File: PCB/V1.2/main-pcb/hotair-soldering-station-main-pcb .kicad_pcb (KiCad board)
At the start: 2 copper layers, 100 x 70 mm, 146 parts, among them J1 230VAC_IN, J10 T12_power (NS-25 r2,54), J11 LCD_CON2 (JST r.2.0), J12 LCD_CON1 (JST r.2.0), J13 ICP (goldpin r2,54), J14 Unused_GPIO, J2 FRONT_PANEL (IDC r. 2,54), J3 EARTH_GND, J4 24V_IN (NS-25 r2,54), J5 PSUPPLY (PWZ-02S r.3,96), J6 HOTAIR_FAN (JST r,2,54), J7 HOTAIR_MEAS (JST r.2,5), J8 HOTAIR_HEATER (PWZ-02S r.3,96), J9 WEP (r.2,54), Q1 BC817, Q10 RFP15P05, Q11 BC817, Q12 BC817, Q13 BC817, Q14 BC807, Q15 RFP15P05, Q2 BC807, Q3 BC817, Q4 RFP15P05, Q5 BC817, Q6 BT139-600, Q7 BC817, Q8 BC807, Q9 BC817, U1 MOC3041M, U2 MAX31855KASA, U3 MP1584-Step-Down, U4 AP1117-ADJ, U5 LM741, U6 AD8606, U8 STM32F103C6Tx

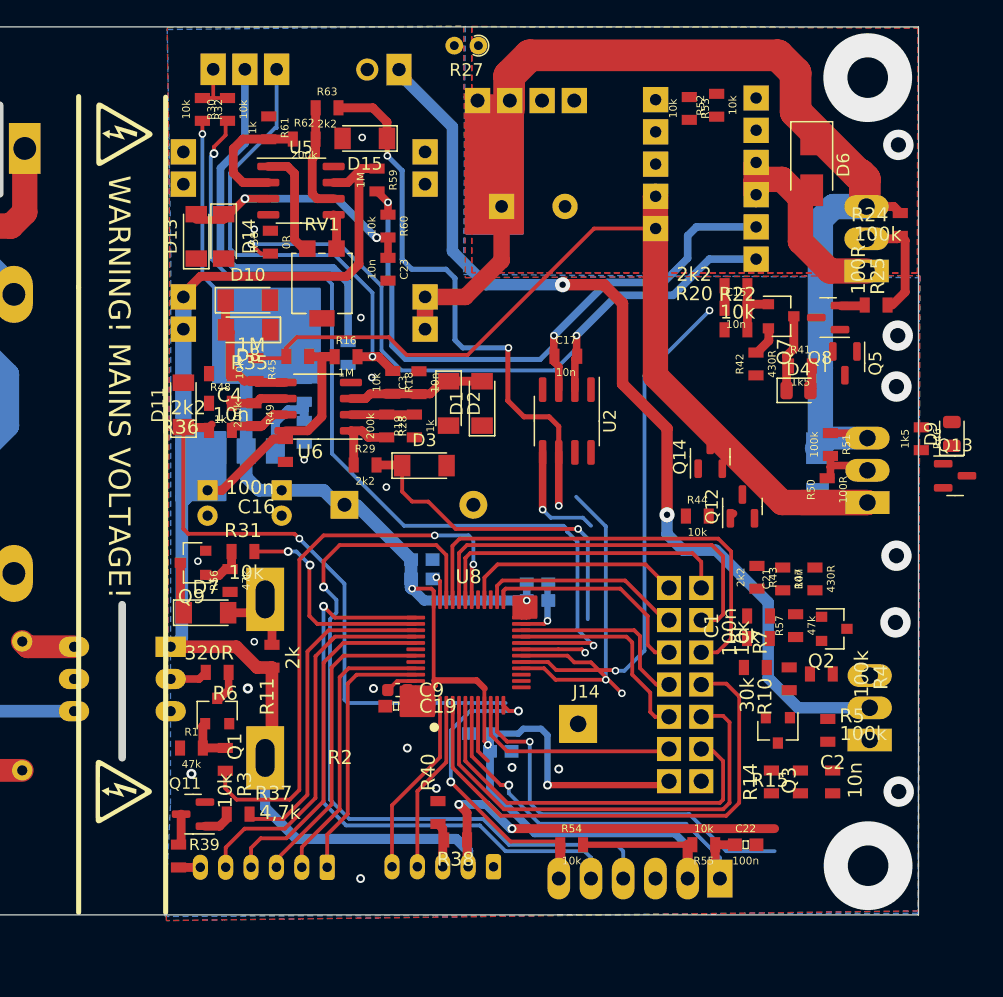
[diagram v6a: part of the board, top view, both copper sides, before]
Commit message: Routing PCB done, resolving DRC violations
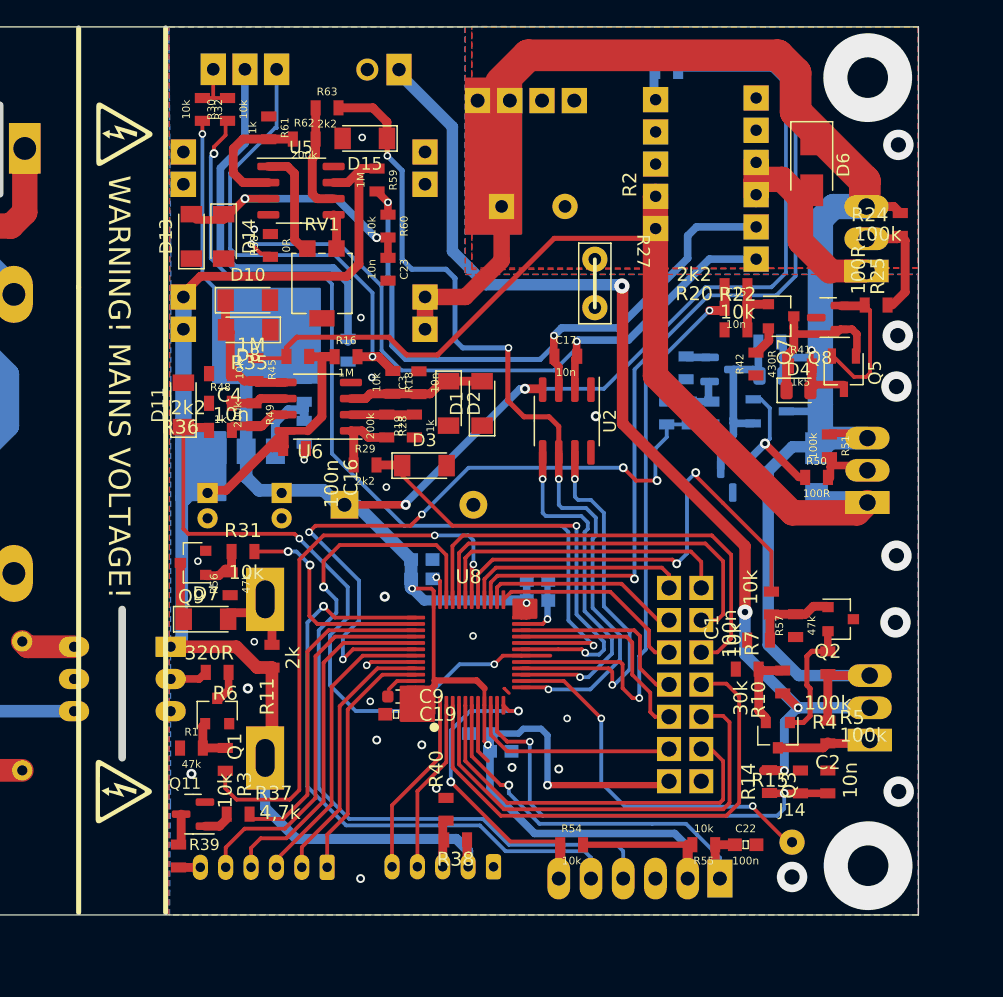
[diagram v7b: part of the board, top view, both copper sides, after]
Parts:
- C21, D9, Q12, Q14, R43, R44, R46, R47, R52, R53: moved to B.Cu
- J14: footprint My-Footprints:WIRE_PAD_1,3mm -> Wire_Pads:SolderWirePad_single_0-8mmDrill
- Q13: footprint Package_TO_SOT_SMD:SOT-23 -> Package_TO_SOT_SMD:TSOT-23; moved to B.Cu
- Q5: footprint Package_TO_SOT_SMD:SOT-23 -> Package_TO_SOT_SMD:TSOT-23
- R27: footprint Resistor_THT:R_Axial_DIN0204_L3.6mm_D1.6mm_P1.90mm_Vertical -> My-Footprints:ShortWire
- moved G*** 43.5 mm to (88.8, 46.6)
- moved G*** 26.4 mm to (76.3, 45.0)
- moved R47 19.5 mm to (98.7, 39.9)
- moved J14 19.3 mm to (107.0, 77.3)
- moved R27 19.2 mm to (91.5, 31.3), turned to -90 degrees
- moved Q13 15.5 mm to (105.3, 43.3)
- moved C21 15.0 mm to (98.9, 43.4)
- moved D9 14.9 mm to (105.4, 40.5), turned to 180 degrees
- moved R43 14.8 mm to (97.2, 43.4)
- moved R46 14.2 mm to (105.3, 37.8), turned to 0 degrees
- moved Q12 10.9 mm to (101.5, 40.0), turned to 0 degrees
- moved R44 8.21 mm to (100.7, 43.4), turned to 90 degrees
- moved R52 4.72 mm to (99.2, 14.9), turned to 180 degrees
- moved R53 3.42 mm to (97.2, 16.5), turned to 0 degrees
- moved Q14 2.59 mm to (102.4, 48.8), turned to -90 degrees
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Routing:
- net IRON_T12_MOTION_SW: track 0.00 -> 68.9 mm, vias 0 -> 1
- net +3V3: track 146.4 -> 214.1 mm, vias 5 -> 7
- net IRON_T12_HEATER_CTRL: track 0.00 -> 54.9 mm, vias 0 -> 5
- net +24V: track 98.6 -> 144.3 mm, vias 0 -> 1
- net HOTAIR_FAN_PWM: track 0.00 -> 37.9 mm, vias 0 -> 2
- net UNUSED_GPIO: track 0.00 -> 30.1 mm, vias 0 -> 2
- net +5V: track 147.5 -> 121.6 mm, vias 2 -> 0
- net MAX31855_IRON_CS: track 45.0 -> 69.3 mm, vias 3 -> 4
- net SPI1_SCK: track 8.85 -> 28.0 mm, vias 1 -> 2
- net Net-(D9-Pad2): track 0.00 -> 15.2 mm
- net Net-(Q13-Pad2): track 0.00 -> 11.5 mm, vias 0 -> 1
- net Net-(Q2-Pad2): track 0.00 -> 10.0 mm
- net Net-(Q5-Pad2): track 1.87 -> 11.2 mm
- net FAN_SUPPLY: track 76.3 -> 84.3 mm, vias 2 -> 4
- net Net-(Q3-Pad3): track 0.00 -> 7.64 mm
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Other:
- outline, holes or cut-outs redrawn
- board text added: "16X2 LCD CONNECTORS"
- board text added: "24V DC INPUT"
- board text added: "HOTAIR HEATER"
- board text added: "HOTAIR THERM/REED"
- board text added: "IN"
- board text added: "MAIN PCB V1.2 05.2022"
- board text added: "OUT"
- board text added: "POWER SUPPLY 230V/24V"
- board text added: "T12"
- board text removed: "24V IN"
- board text removed: "HOTAIR"
- board text removed: "HOTAIR SIGNAL"
- board text removed: "LCD CON1"
- board text removed: "LCD CON2"
- board text removed: "LED BCL"
- board text removed: "MAIN PCB V1.1 02.2022"
- board text removed: "POWER SUPPLY"
- board text removed: "T12 POWER"
- board text removed: "T12 SIGNAL"

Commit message: Silkscreen progress
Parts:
- C12: footprint Capacitors:0603 -> Capacitors:0805
- moved G*** 0.49 mm to (76.5, 44.5)
- moved C12 0.41 mm to (84.1, 70.5)
- moved C16 0.05 mm to (67.8, 46.2)
